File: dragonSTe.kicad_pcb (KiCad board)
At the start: 4 copper layers, 310 parts, among them J2 MIDI OUT, J3 MIDI IN, J4 DB25_Socket, J5 DB25_Pins, J6 Keyboard, J7 Internal FDD, Q1 2N3904, Q10 2N3904, Q2 2N3904, Q3 2N3904, Q4 2N3904, Q5 2N3904, Q6 2N3904, Q7 2N3904, Q8 2N3904, Q9 2N3904, SW1 RESET, U1 68000, U10 MC68901, U13 74LS04, U2 27C010, U22 74LS05, U3 27C010, U30 LF347DT, U32 LF347DT, U33 LM78L82, U34 LMC1992, U37 DMA, U38 WD1772, U39 STB, U40 GST_SHIFTER, U42 GST_MCU, U45 74LS04, U5 LM555xM, U6 74LS05, U7 MC6850, U8 MC6850, U9 YM2149, X1 8.010613MHz

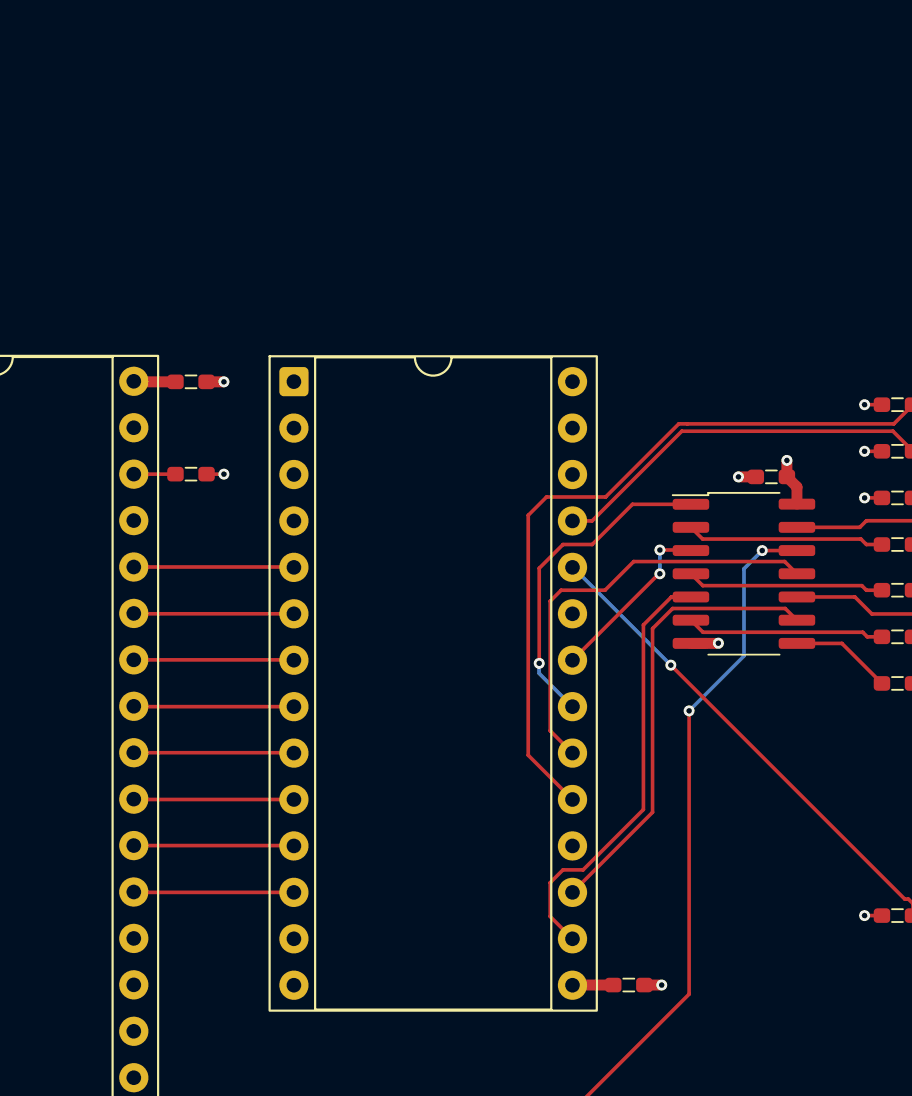
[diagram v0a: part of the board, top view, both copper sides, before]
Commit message: motherboard: Fixed the floppy power connector and defined the board parameters for manufacture
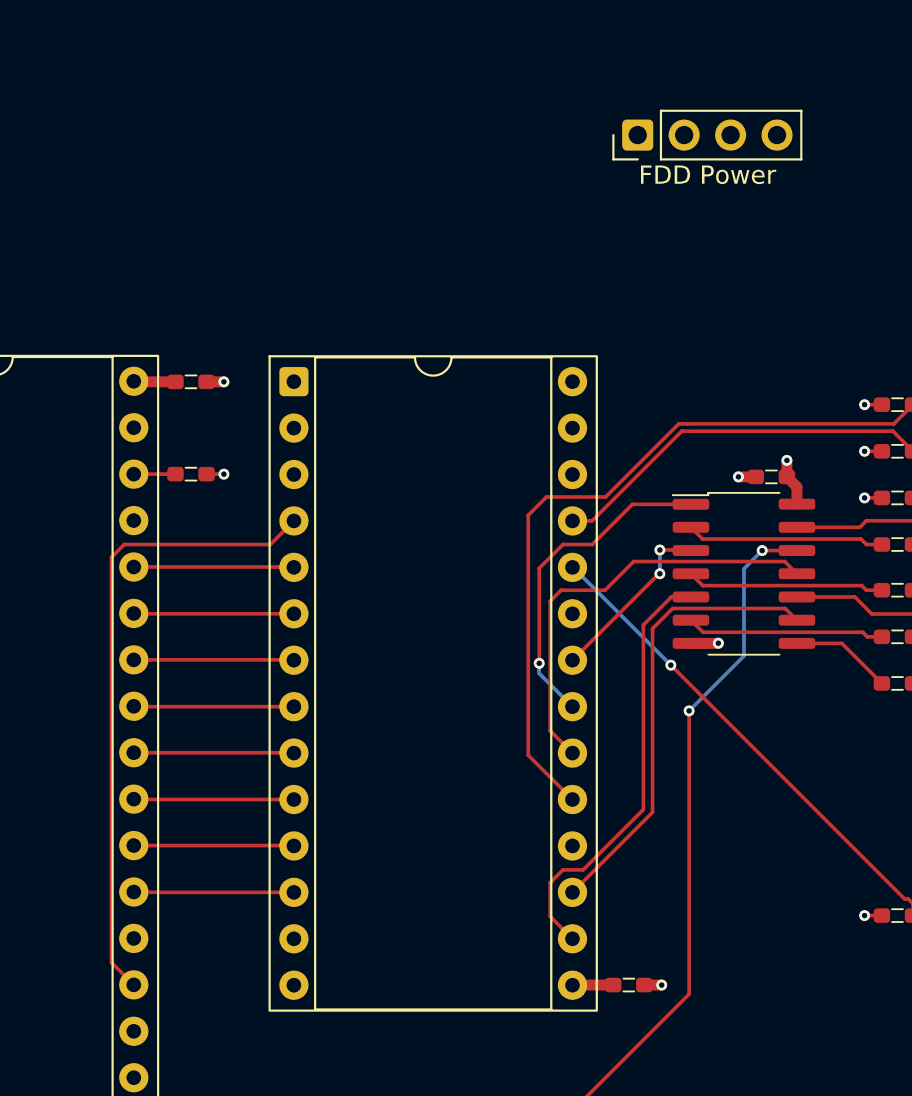
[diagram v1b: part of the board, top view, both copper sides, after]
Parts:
- added J13: FDD Power, rhais_connector-pinheader:PinHeader_1x04_P2.54mm_Vertical, F.Cu at (355.0, 180.0)
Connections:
- U9 pad 39: unconnected-(U9-TEST1-Pad39) -> GND
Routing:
- net Net-(U37-CA2): track 0.00 -> 34.7 mm

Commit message: motherboard: Fixed a pile of resistor network issues, and concluded initial routing of the CPU and audio amp passives
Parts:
- R133, R134: footprint rhais_rcl:R0603 -> rhais_rcl:R0402
- RN1, RN10, RN11, RN12, RN2, RN3, RN4, RN5, RN6, RN7, RN8, RN9: moved to B.Cu
- RN22, RN23, RN24, RN25: footprint rhais_rcl:R0603_Array_Concave_4 -> rhais_rcl:R0402_Array_Convex_4
- U1: footprint Package_DIP:DIP-64_W22.86mm_Socket -> rhais_package-dip:DIP-64_W22.86mm_Socket
- U40: footprint Package_LCC:PLCC-84_SMD-Socket -> rhais_package-plcc:PLCC-84_SMD-Socket
- U42: footprint Package_QFP:LQFP-144_20x20mm_P0.5mm -> rhais_package-qfp:LQFP-144_20x20mm_P0.5mm
- moved Q6 190.6 mm to (228.0, 244.7)
- moved RN9 188.8 mm to (61.9, 117.0), turned to 90 degrees
- moved Q7 180.5 mm to (228.0, 239.5)
- moved RN8 175.4 mm to (72.0, 117.0), turned to 90 degrees
- moved Q8 170.5 mm to (228.0, 234.3)
- moved RN10 166.1 mm to (67.0, 103.0), turned to -90 degrees
- moved RN7 162.1 mm to (82.2, 117.0), turned to 90 degrees
- moved Q9 161.9 mm to (228.0, 230.5)
- moved RN6 148.9 mm to (92.3, 117.0), turned to 90 degrees
- moved U40 136.7 mm to (200.0, 240.0), turned to 90 degrees
- moved RN5 134.6 mm to (103.8, 117.0), turned to 90 degrees
- moved RN11 114.7 mm to (122.8, 103.0), turned to -90 degrees
- moved R65 105.5 mm to (92.3, 237.1), turned to -90 degrees
- moved R66 101.8 mm to (93.2, 234.8), turned to 180 degrees
- moved C87 100.9 mm to (92.3, 240.2), turned to 90 degrees
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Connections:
- RN1 pad 2: +5V -> /CPU+ROMs/SysBus.D15
- RN1 pad 4: +5V -> /CPU+ROMs/SysBus.D14
- RN1 pad 5: /CPU+ROMs/SysBus.D12 -> +5V
- RN1 pad 7: /CPU+ROMs/SysBus.D14 -> +5V
- RN1 pad 8: /CPU+ROMs/SysBus.D15 -> /CPU+ROMs/SysBus.D12
- RN10 pad 1: +5V -> /CPU+ROMs/SysBus.A3
- RN10 pad 3: +5V -> /CPU+ROMs/SysBus.A2
- RN10 pad 5: unconnected-(RN10-R4.2-Pad5) -> /CPU+ROMs/SysBus.A1
- RN10 pad 6: /CPU+ROMs/SysBus.A1 -> +5V
- RN10 pad 7: /CPU+ROMs/SysBus.A2 -> unconnected-(RN10-R2.2-Pad7)
- RN10 pad 8: /CPU+ROMs/SysBus.A3 -> +5V
- RN11 pad 1: +5V -> /CPU+ROMs/SysBus.R/~{W}
- RN11 pad 3: +5V -> /CPU+ROMs/SysBus.~{LDS}
- RN11 pad 5: /CPU+ROMs/SysBus.~{AS} -> /CPU+ROMs/SysBus.~{UDS}
- RN11 pad 6: /CPU+ROMs/SysBus.~{UDS} -> +5V
- RN11 pad 7: /CPU+ROMs/SysBus.~{LDS} -> /CPU+ROMs/SysBus.~{AS}
- RN11 pad 8: /CPU+ROMs/SysBus.R/~{W} -> +5V
- RN12 pad 2: +5V -> /CPU+ROMs/~{BGACK}
- RN12 pad 4: +5V -> /CPU+ROMs/~{BR}
- RN12 pad 5: /CPU+ROMs/~{BR} -> +5V
- RN12 pad 7: /CPU+ROMs/~{BGACK} -> +5V
- RN15 pad 2: /Disk & Floppy/~{HDACK} -> Net-(RN15-R2.1)
- RN15 pad 3: /Disk & Floppy/HDA0 -> /Disk & Floppy/~{HDACK}
- RN15 pad 4: /Disk & Floppy/HDR/~{W} -> Net-(RN15-R4.1)
- RN15 pad 5: Net-(RN15-R4.2) -> /Disk & Floppy/HDA0
- RN15 pad 7: Net-(RN15-R2.2) -> /Disk & Floppy/HDR/~{W}
- RN16 pad 2: +5V -> Net-(RN16-R2.1)
- RN16 pad 4: +5V -> Net-(RN16-R4.1)
- RN16 pad 5: Net-(RN16-R4.2) -> +5V
- RN16 pad 7: Net-(RN16-R2.2) -> +5V
- RN17 pad 2: +5V -> Net-(RN17-R2.1)
- RN17 pad 4: +5V -> Net-(RN17-R4.1)
- RN17 pad 5: Net-(RN17-R4.2) -> +5V
- RN17 pad 7: Net-(RN17-R2.2) -> +5V
- RN18 pad 2: Net-(RN18-R2.1) -> +5V
- RN18 pad 4: Net-(RN18-R4.1) -> +5V
- RN18 pad 5: +5V -> Net-(RN18-R4.2)
- RN18 pad 7: +5V -> Net-(RN18-R2.2)
- RN19 pad 2: Net-(RN19-R2.1) -> +5V
- RN19 pad 4: Net-(RN19-R4.1) -> +5V
- RN19 pad 5: +5V -> Net-(RN19-R4.2)
- RN19 pad 7: +5V -> Net-(RN19-R2.2)
- RN2 pad 2: +5V -> /CPU+ROMs/SysBus.D11
- RN2 pad 4: +5V -> /CPU+ROMs/SysBus.D10
- RN2 pad 5: /CPU+ROMs/SysBus.D8 -> +5V
- RN2 pad 7: /CPU+ROMs/SysBus.D10 -> +5V
- RN2 pad 8: /CPU+ROMs/SysBus.D11 -> /CPU+ROMs/SysBus.D8
- RN20 pad 2: Net-(RN20-R2.1) -> +5V
- RN20 pad 4: Net-(RN20-R4.1) -> +5V
- RN20 pad 5: +5V -> Net-(RN20-R4.2)
- RN20 pad 7: +5V -> Net-(RN20-R2.2)
- RN21 pad 2: Net-(RN21-R2.1) -> +5V
- RN21 pad 4: Net-(RN21-R4.1) -> +5V
- RN21 pad 5: +5V -> Net-(RN21-R4.2)
- RN21 pad 7: +5V -> Net-(RN21-R2.2)
- RN22 pad 1: /RAM/RAM.A9 -> Net-(RN22-R1.1)
- RN22 pad 2: /RAM/RAM.A8 -> /RAM/RAM.A9
- RN22 pad 3: /RAM/RAM.A7 -> Net-(RN22-R3.1)
- RN22 pad 4: /RAM/RAM.A6 -> /RAM/RAM.A8
- RN22 pad 6: Net-(RN22-R3.2) -> /RAM/RAM.A7
- RN22 pad 8: Net-(RN22-R1.2) -> /RAM/RAM.A6
- RN23 pad 1: /RAM/RAM.A5 -> Net-(RN23-R1.1)
- RN23 pad 2: /RAM/RAM.A4 -> /RAM/RAM.A5
- RN23 pad 3: /RAM/RAM.A3 -> Net-(RN23-R3.1)
- RN23 pad 4: /RAM/RAM.A2 -> /RAM/RAM.A4
- RN23 pad 6: Net-(RN23-R3.2) -> /RAM/RAM.A3
- RN23 pad 8: Net-(RN23-R1.2) -> /RAM/RAM.A2
- RN24 pad 2: /RAM/RAM.~{CASL1} -> Net-(RN24-R2.1)
- RN24 pad 3: /RAM/RAM.~{CASH1} -> /RAM/RAM.~{CASL1}
- RN24 pad 4: /RAM/RAM.~{RAS1} -> Net-(RN24-R4.1)
- RN24 pad 5: Net-(RN24-R4.2) -> /RAM/RAM.~{CASH1}
- RN24 pad 7: Net-(RN24-R2.2) -> /RAM/RAM.~{RAS1}
- RN25 pad 2: /RAM/RAM.~{CASH0} -> Net-(RN25-R2.1)
- RN25 pad 3: /RAM/RAM.~{RAS0} -> /RAM/RAM.~{CASH0}
- RN25 pad 4: unconnected-(RN25-R4.1-Pad4) -> Net-(RN25-R4.1)
- RN25 pad 5: unconnected-(RN25-R4.2-Pad5) -> /RAM/RAM.~{RAS0}
- RN25 pad 7: Net-(RN25-R2.2) -> unconnected-(RN25-R2.2-Pad7)
- RN25 pad 8: Net-(RN25-R1.2) -> unconnected-(RN25-R1.2-Pad8)
- RN26 pad 2: +5V -> Net-(JP3-B)
- RN26 pad 4: +5V -> Net-(JP7-B)
- RN26 pad 5: Net-(JP8-B) (its old number) -> +5V
- RN26 pad 7: Net-(JP7-B) -> +5V
- RN27 pad 2: +5V -> Net-(JP5-B)
- RN27 pad 4: +5V -> Net-(JP9-B)
- RN27 pad 5: Net-(JP10-B) (its old number) -> +5V
- RN27 pad 7: Net-(JP9-B) -> +5V
- RN3 pad 2: +5V -> /CPU+ROMs/SysBus.D7
- RN3 pad 4: +5V -> /CPU+ROMs/SysBus.D6
- RN3 pad 5: /CPU+ROMs/SysBus.D4 -> +5V
- RN3 pad 7: /CPU+ROMs/SysBus.D6 -> +5V
- RN3 pad 8: /CPU+ROMs/SysBus.D7 -> /CPU+ROMs/SysBus.D4
- RN4 pad 2: +5V -> /CPU+ROMs/SysBus.D3
- RN4 pad 4: +5V -> /CPU+ROMs/SysBus.D2
- RN4 pad 5: /CPU+ROMs/SysBus.D0 -> +5V
- RN4 pad 7: /CPU+ROMs/SysBus.D2 -> +5V
- RN4 pad 8: /CPU+ROMs/SysBus.D3 -> /CPU+ROMs/SysBus.D0
- RN5 pad 1: +5V -> /CPU+ROMs/SysBus.A23
- RN5 pad 3: +5V -> /CPU+ROMs/SysBus.A22
- RN5 pad 5: /CPU+ROMs/SysBus.A20 -> /CPU+ROMs/SysBus.A21
- RN5 pad 6: /CPU+ROMs/SysBus.A21 -> +5V
- RN5 pad 7: /CPU+ROMs/SysBus.A22 -> /CPU+ROMs/SysBus.A20
- RN5 pad 8: /CPU+ROMs/SysBus.A23 -> +5V
- RN6 pad 1: +5V -> /CPU+ROMs/SysBus.A19
- RN6 pad 3: +5V -> /CPU+ROMs/SysBus.A18
- RN6 pad 5: /CPU+ROMs/SysBus.A16 -> /CPU+ROMs/SysBus.A17
- RN6 pad 6: /CPU+ROMs/SysBus.A17 -> +5V
- RN6 pad 7: /CPU+ROMs/SysBus.A18 -> /CPU+ROMs/SysBus.A16
- RN6 pad 8: /CPU+ROMs/SysBus.A19 -> +5V
- RN7 pad 1: +5V -> /CPU+ROMs/SysBus.A15
- RN7 pad 3: +5V -> /CPU+ROMs/SysBus.A14
- RN7 pad 5: /CPU+ROMs/SysBus.A12 -> /CPU+ROMs/SysBus.A13
- RN7 pad 6: /CPU+ROMs/SysBus.A13 -> +5V
- RN7 pad 7: /CPU+ROMs/SysBus.A14 -> /CPU+ROMs/SysBus.A12
- RN7 pad 8: /CPU+ROMs/SysBus.A15 -> +5V
- RN8 pad 1: +5V -> /CPU+ROMs/SysBus.A11
- RN8 pad 3: +5V -> /CPU+ROMs/SysBus.A10
- RN8 pad 5: /CPU+ROMs/SysBus.A8 -> /CPU+ROMs/SysBus.A9
- RN8 pad 6: /CPU+ROMs/SysBus.A9 -> +5V
- RN8 pad 7: /CPU+ROMs/SysBus.A10 -> /CPU+ROMs/SysBus.A8
- RN8 pad 8: /CPU+ROMs/SysBus.A11 -> +5V
- RN9 pad 1: +5V -> /CPU+ROMs/SysBus.A7
- RN9 pad 3: +5V -> /CPU+ROMs/SysBus.A6
- RN9 pad 5: /CPU+ROMs/SysBus.A4 -> /CPU+ROMs/SysBus.A5
- RN9 pad 6: /CPU+ROMs/SysBus.A5 -> +5V
- RN9 pad 7: /CPU+ROMs/SysBus.A6 -> /CPU+ROMs/SysBus.A4
- RN9 pad 8: /CPU+ROMs/SysBus.A7 -> +5V
- U42 pad 112: Net-(RN23-R4.2) -> Net-(RN23-R2.2)
- U42 pad 113: Net-(RN23-R3.2) -> Net-(RN23-R4.2)
- U42 pad 114: Net-(RN23-R2.2) -> Net-(RN23-R3.1)
- U42 pad 115: Net-(RN23-R1.2) -> Net-(RN23-R1.1)
- U42 pad 116: Net-(RN22-R4.2) -> Net-(RN22-R2.2)
- U42 pad 117: Net-(RN22-R3.2) -> Net-(RN22-R4.2)
- U42 pad 118: Net-(RN22-R2.2) -> Net-(RN22-R3.1)
- U42 pad 119: Net-(RN22-R1.2) -> Net-(RN22-R1.1)
- U42 pad 121: Net-(RN24-R1.2) -> Net-(RN24-R2.1)
- U42 pad 122: Net-(RN24-R2.2) -> Net-(RN24-R4.1)
- U42 pad 124: Net-(RN24-R4.2) -> Net-(RN24-R1.2)
- U42 pad 125: Net-(RN25-R1.2) -> Net-(RN25-R2.1)
- U42 pad 126: Net-(RN25-R2.2) -> Net-(RN25-R4.1)
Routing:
- net Net-(U37-FDRQ): track 0.00 -> 59.7 mm, vias 0 -> 2
- net Net-(U37-~{FDCS}): track 0.00 -> 54.9 mm, vias 0 -> 2
- net Net-(U19-I3a): track 0.00 -> 45.0 mm
- net GND: track 10.0 -> 30.8 mm, vias 10 -> 20
- net /CPU+ROMs/SysBus.A4: track 19.4 -> 39.2 mm
- net /CPU+ROMs/SysBus.D4: track 0.00 -> 19.8 mm
- net /CPU+ROMs/~{BUS_ERR}: track 0.00 -> 14.3 mm
- net /CPU+ROMs/~{BGACK}: track 0.00 -> 12.4 mm
- net /CPU+ROMs/~{BR}: track 0.00 -> 10.6 mm
- net Net-(U32D--): track 0.00 -> 10.6 mm
- net Net-(U32C--): track 0.00 -> 10.6 mm
- net Net-(C76-Pad1): track 0.00 -> 6.65 mm
- net Net-(C80-Pad1): track 0.00 -> 6.64 mm
- net Net-(U32B--): track 0.00 -> 6.20 mm
- net Net-(U32A--): track 0.00 -> 6.20 mm
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- added copper zone on In2.Cu, net +5V
- added copper zone on In1.Cu, net GND

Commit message: motherboard: Added packaging and ordering information for many of the 7400 logic parts and the DACs
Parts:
- C67, C68, C69, C70, C72, C73, C85, C86: moved to B.Cu
- U34: footprint Package_DIP:DIP-28_W15.24mm_Socket -> rhais_package-dip:DIP-28_W15.24mm_Socket
- moved R88 254.2 mm to (360.0, 240.0)
- moved R73 199.3 mm to (75.8, 44.9), turned to 90 degrees
- moved R72 196.0 mm to (77.6, 44.9), turned to 90 degrees
- moved C87 195.8 mm to (78.9, 44.9), turned to -90 degrees
- moved C92 194.0 mm to (76.7, 47.0), turned to 180 degrees
- moved R55 192.8 mm to (56.4, 52.4), turned to 180 degrees
- moved C76 190.8 mm to (58.5, 51.5), turned to -90 degrees
- moved R65 189.6 mm to (78.9, 48.0), turned to 90 degrees
- moved R60 189.3 mm to (56.4, 57.6), turned to 180 degrees
- moved R56 189.2 mm to (59.9, 51.5), turned to -90 degrees
- moved C75 188.7 mm to (59.0, 53.7), turned to 0 degrees
- moved C81 186.9 mm to (59.0, 56.3), turned to 0 degrees
- moved C61 186.5 mm to (83.8, 49.2), turned to 90 degrees
- moved R47 186.5 mm to (85.1, 49.2), turned to -90 degrees
- moved C80 186.0 mm to (58.5, 58.5), turned to 90 degrees
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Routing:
- net /DAC + Joysticks/GIR: track 0.00 -> 45.4 mm
- net /DAC + Joysticks/GIL: track 0.00 -> 42.8 mm
- net Net-(U34-RSEL_IN): track 0.00 -> 41.9 mm
- net Net-(U34-LSEL_IN): track 0.00 -> 39.3 mm
- net Net-(U34-LIN1): track 0.00 -> 24.8 mm
- net Net-(U34-LIN2): track 0.00 -> 18.6 mm
- net Net-(U34-RF_OUT): track 1.30 -> 16.0 mm
- net Net-(U34-LF_OUT): track 1.30 -> 13.5 mm
- net GND: track 30.8 -> 39.0 mm, vias 20 -> 26
- net Net-(C93-Pad1): track 0.00 -> 7.90 mm
- net /DAC + Joysticks/AUDIOS: track 20.1 -> 26.2 mm
- net /DAC + Joysticks/-5VA: track 0.00 -> 4.90 mm, vias 0 -> 2
- net /DAC + Joysticks/+5VA: track 0.00 -> 2.45 mm, vias 0 -> 1
- net /DAC + Joysticks/+8V2: track 0.00 -> 2.45 mm, vias 0 -> 1
- net Net-(U34-LTONE_IN): track 0.00 -> 2.42 mm
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
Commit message: motherboard: Routed out the bulk of the DAC section and feed latches
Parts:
- added J8: JOY0, Connector_Dsub:DSUB-15_Socket_Horizontal_P2.77x2.54mm_EdgePinOffset9.40mm, F.Cu at (-22.0, 68.8)
- added J9: JOY1, Connector_Dsub:DSUB-15_Socket_Horizontal_P2.77x2.54mm_EdgePinOffset9.40mm, F.Cu at (-22.0, 46.9)
- added U15: 74HC86, rhais_package-smd:SO-14_3.9x8.65mm_P1.27mm, F.Cu at (369.9, 145.3)
- added U18: 74HC74, rhais_package-smd:SO-14_3.9x8.65mm_P1.27mm, F.Cu at (328.5, 147.4)
- added U19: 74HC244, rhais_package-smd:SO-20_12.8x7.5mm_P1.27mm, F.Cu at (330.0, 135.0)
- added U20: 74HC245, rhais_package-smd:SO-20_12.8x7.5mm_P1.27mm, F.Cu at (342.4, 135.0)
- added U21: 74HC74, rhais_package-smd:SO-14_3.9x8.65mm_P1.27mm, F.Cu at (337.9, 147.4)
- added U23: 74HC374, rhais_package-smd:SO-20_12.8x7.5mm_P1.27mm, F.Cu at (45.0, 61.0)
- added U24: 74HC374, rhais_package-smd:SO-20_12.8x7.5mm_P1.27mm, F.Cu at (45.0, 49.0)
- added U25: 74HC244, rhais_package-smd:SO-20_12.8x7.5mm_P1.27mm, F.Cu at (337.6, 110.0)
- added U26: 74HC244, rhais_package-smd:SO-20_12.8x7.5mm_P1.27mm, F.Cu at (350.0, 110.0)
- added U27: 74HC373, rhais_package-smd:SO-20_12.8x7.5mm_P1.27mm, F.Cu at (362.4, 110.0)
- added U28: 74HC244, rhais_package-smd:SO-20_12.8x7.5mm_P1.27mm, F.Cu at (374.9, 110.0)
- added U29: DAC0802, rhais_package-smd:SO-16_3.9x9.9mm_P1.27mm, F.Cu at (64.7, 43.0)
- added U31: DAC0802, rhais_package-smd:SO-16_3.9x9.9mm_P1.27mm, F.Cu at (64.7, 67.0)
- added U4: 74HC74, rhais_package-smd:SO-14_3.9x8.65mm_P1.27mm, F.Cu at (381.3, 132.9)
- added U43: 74HC244, rhais_package-smd:SO-20_12.8x7.5mm_P1.27mm, F.Cu at (356.9, 135.0)
- added U44: 74HC86, rhais_package-smd:SO-14_3.9x8.65mm_P1.27mm, F.Cu at (369.9, 132.9)
- U13, U45: value 74LS04 -> 74HCT14D
- U22, U6: value 74LS05 -> 74HS05
- moved R44 174.3 mm to (59.0, 44.9)
- moved R43 171.4 mm to (59.0, 46.2)
- moved R45 170.9 mm to (70.5, 43.6), turned to 180 degrees
- moved C70 170.2 mm to (62.1, 43.7), turned to 0 degrees
- moved C69 167.0 mm to (67.3, 44.8), turned to 180 degrees
- moved C66 163.2 mm to (59.0, 47.5), turned to 180 degrees
- moved C71 153.1 mm to (59.0, 71.5), turned to 180 degrees
- moved C72 149.2 mm to (62.1, 67.8), turned to 0 degrees
- moved C73 145.7 mm to (67.3, 68.8), turned to 180 degrees
- moved R51 144.0 mm to (59.0, 70.2)
- moved R50 143.3 mm to (59.0, 68.9)
- moved R52 139.3 mm to (70.5, 67.6), turned to 180 degrees
- moved R53 15.3 mm to (70.5, 70.2), turned to 180 degrees
- moved R46 12.4 mm to (70.5, 46.2), turned to 180 degrees
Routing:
- net Net-(U24-O0): track 0.00 -> 37.5 mm, vias 0 -> 2
- net Net-(U24-O1): track 0.00 -> 35.1 mm, vias 0 -> 2
- net Net-(U24-O2): track 0.00 -> 34.8 mm, vias 0 -> 2
- net Net-(U24-O3): track 0.00 -> 32.3 mm
- net Net-(U24-O7): track 0.00 -> 22.9 mm, vias 0 -> 2
- net Net-(U30D-+): track 2.01 -> 24.2 mm, vias 0 -> 2
- net Net-(U24-O6): track 0.00 -> 20.6 mm, vias 0 -> 2
- net Net-(U24-O5): track 0.00 -> 20.0 mm, vias 0 -> 2
- net Net-(U24-O4): track 0.00 -> 17.6 mm
- net Net-(U29-~{I_{OUT}}): track 2.01 -> 18.9 mm, vias 0 -> 2
- net /DAC + Joysticks/Sound.D3: track 0.00 -> 12.6 mm
- net /DAC + Joysticks/Sound.D4: track 0.00 -> 12.5 mm
- net /DAC + Joysticks/Sound.D0: track 0.00 -> 12.5 mm
- net /DAC + Joysticks/Sound.D6: track 0.00 -> 12.5 mm
- net /DAC + Joysticks/Sound.D2: track 0.00 -> 12.5 mm
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
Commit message: motherboard: Routing for the joystick ports
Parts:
- RN21: moved to B.Cu
- moved U28 312.3 mm to (90.0, 238.0), turned to 90 degrees
- moved U27 296.1 mm to (90.0, 226.0), turned to 90 degrees
- moved U26 280.0 mm to (90.0, 214.0), turned to 90 degrees
- moved U25 264.1 mm to (90.0, 202.0), turned to 90 degrees
- moved J9 222.5 mm to (68.6, 250.2), turned to -90 degrees
- moved RN21 180.3 mm to (81.0, 203.0), turned to 180 degrees
- moved J8 167.1 mm to (68.6, 209.2), turned to -90 degrees
- moved RN18 146.5 mm to (73.0, 246.1)
- moved RN17 138.9 mm to (73.0, 239.1)
- moved RN19 122.8 mm to (73.0, 205.1)
- moved RN16 109.9 mm to (73.0, 198.1)
- moved C60 92.6 mm to (82.7, 234.7), turned to -90 degrees
- moved C59 86.1 mm to (82.7, 222.7), turned to -90 degrees
- moved C58 80.3 mm to (82.7, 210.7), turned to -90 degrees
- moved C57 75.2 mm to (82.7, 198.7), turned to -90 degrees
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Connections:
- J8 pad 11: Net-(RN16-R1.2) -> Net-(RN16-R2.2)
- J8 pad 12: Net-(RN16-R3.2) -> Net-(RN16-R4.2)
- J8 pad 13: Net-(RN16-R4.1) -> Net-(RN16-R3.1)
- J8 pad 14: Net-(RN16-R2.1) -> Net-(RN16-R1.1)
- J9 pad 11: Net-(RN17-R1.2) -> Net-(RN17-R2.2)
- J9 pad 12: Net-(RN17-R3.2) -> Net-(RN17-R4.2)
- J9 pad 13: Net-(RN17-R4.1) -> Net-(RN17-R3.1)
- J9 pad 14: Net-(RN17-R2.1) -> Net-(RN17-R1.1)
- RN16 pad 1: +5V -> Net-(RN16-R1.1)
- RN16 pad 2: Net-(RN16-R2.1) -> +5V
- RN16 pad 3: +5V -> Net-(RN16-R3.1)
- RN16 pad 4: Net-(RN16-R4.1) -> +5V
- RN16 pad 5: +5V -> Net-(RN16-R4.2)
- RN16 pad 6: Net-(RN16-R3.2) -> +5V
- RN16 pad 7: +5V -> Net-(RN16-R2.2)
- RN16 pad 8: Net-(RN16-R1.2) -> +5V
- RN17 pad 1: +5V -> Net-(RN17-R1.1)
- RN17 pad 2: Net-(RN17-R2.1) -> +5V
- RN17 pad 3: +5V -> Net-(RN17-R3.1)
- RN17 pad 4: Net-(RN17-R4.1) -> +5V
- RN17 pad 5: +5V -> Net-(RN17-R4.2)
- RN17 pad 6: Net-(RN17-R3.2) -> +5V
- RN17 pad 7: +5V -> Net-(RN17-R2.2)
- RN17 pad 8: Net-(RN17-R1.2) -> +5V
- U28 pad 11: Net-(RN17-R2.1) -> Net-(RN17-R1.1)
- U28 pad 13: Net-(RN17-R4.1) -> Net-(RN17-R3.1)
- U28 pad 15: Net-(RN17-R3.2) -> Net-(RN17-R4.2)
- U28 pad 17: Net-(RN17-R1.2) -> Net-(RN17-R2.2)
- U28 pad 2: Net-(RN16-R2.1) -> Net-(RN16-R1.1)
- U28 pad 4: Net-(RN16-R4.1) -> Net-(RN16-R3.1)
- U28 pad 6: Net-(RN16-R3.2) -> Net-(RN16-R4.2)
- U28 pad 8: Net-(RN16-R1.2) -> Net-(RN16-R2.2)
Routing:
- net /CPU+ROMs/SysBus.D1: track 3.95 -> 30.0 mm
- net /CPU+ROMs/SysBus.D0: track 4.67 -> 30.3 mm
- net /CPU+ROMs/SysBus.D3: track 4.65 -> 30.2 mm, vias 0 -> 2
- net /CPU+ROMs/SysBus.D7: track 4.66 -> 28.7 mm, vias 0 -> 2
- net /CPU+ROMs/SysBus.D4: track 19.8 -> 36.7 mm, vias 0 -> 2
- net Net-(RN18-R1.1): track 0.00 -> 15.5 mm, vias 0 -> 2
- net Net-(RN18-R4.2): track 0.00 -> 13.6 mm
- net Net-(RN18-R3.1): track 0.00 -> 13.6 mm, vias 0 -> 2
- net Net-(RN19-R2.2): track 0.00 -> 13.0 mm
- net Net-(RN19-R3.1): track 0.00 -> 13.0 mm
- net Net-(RN19-R4.2): track 0.00 -> 12.5 mm
- net +5V: track 33.3 -> 45.3 mm, vias 17 -> 21
- net /CPU+ROMs/SysBus.D6: track 3.94 -> 14.8 mm, vias 0 -> 1
- net /CPU+ROMs/SysBus.D5: track 3.94 -> 14.2 mm, vias 0 -> 1
- net /DAC + Joysticks/~{JOY_RL}: track 0.00 -> 9.93 mm
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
